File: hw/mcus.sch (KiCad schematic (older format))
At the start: 47 parts, among them P15 CONN_1, P16 CONN_1, P18 CONN_1, U10 MPU-6000, U11 HMC5983, U7 STM32F405VG, U8 STM32F303CC, U9 MS5611, X1 8MHz, X2 8MHz

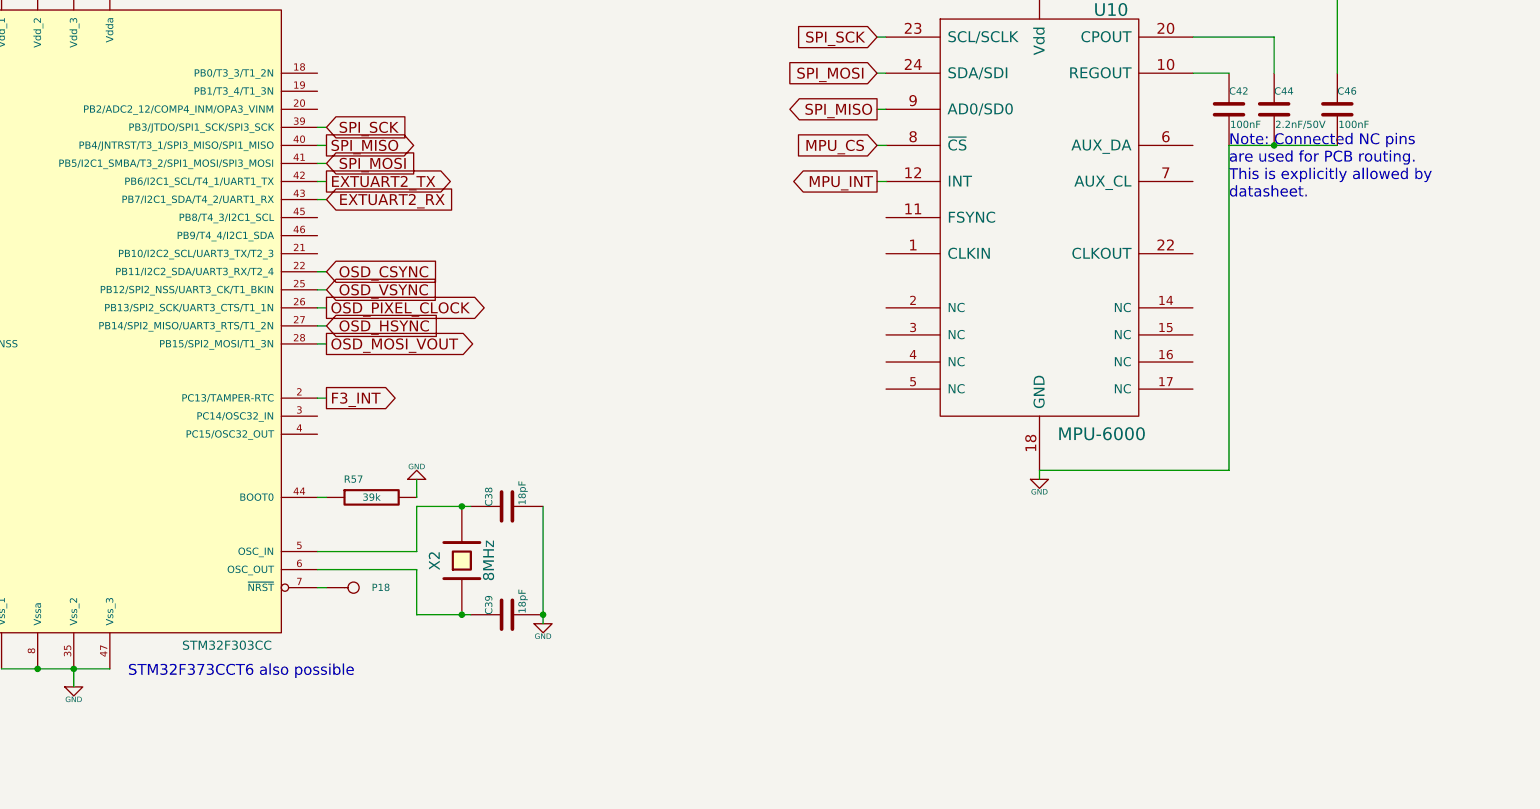
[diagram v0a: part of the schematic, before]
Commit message: Just cosmetic changes for eye-candy, no changes in board layout
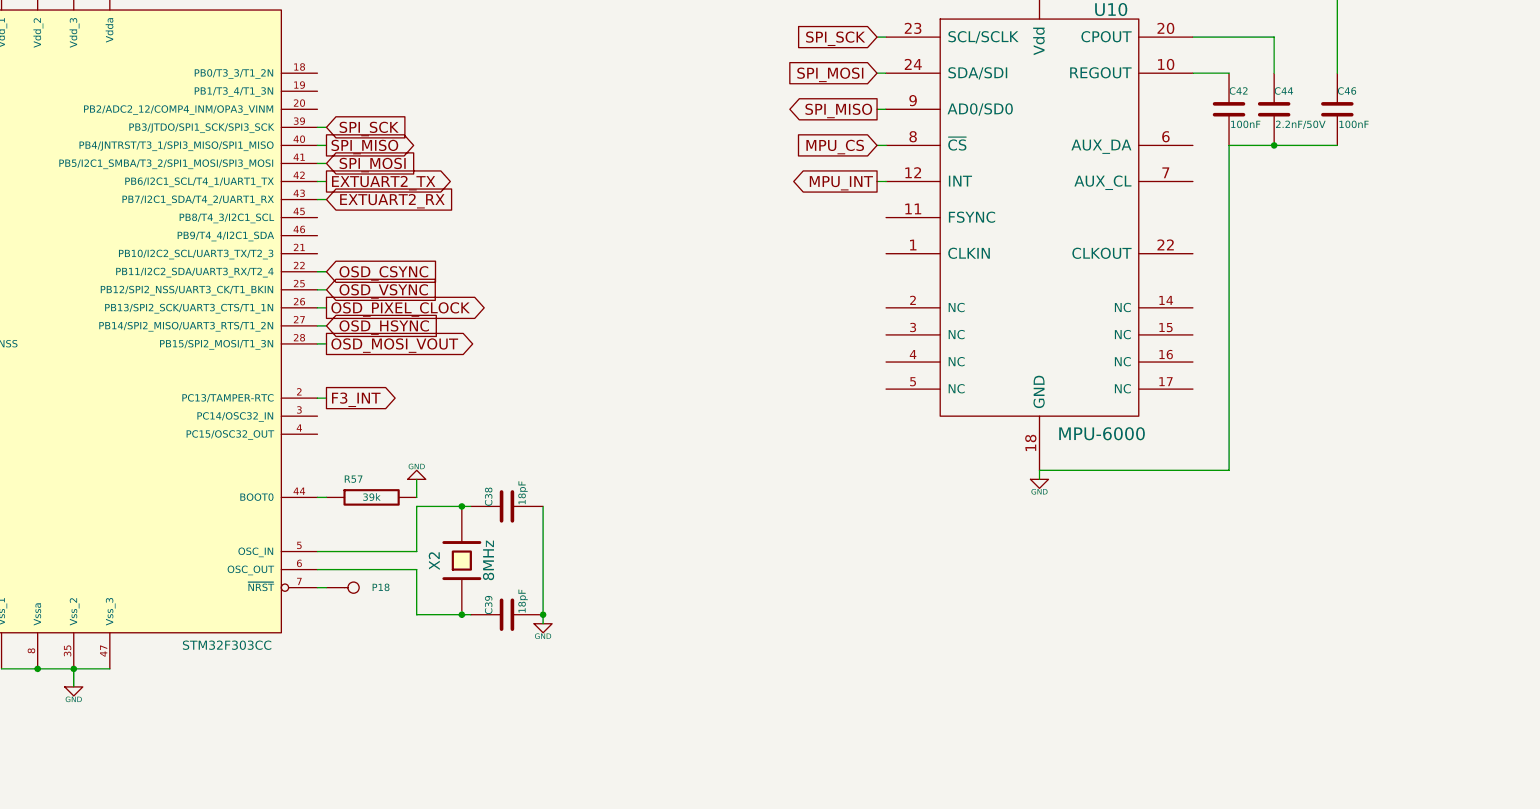
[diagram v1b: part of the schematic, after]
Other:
- note removed: "Note: Connected NC pins\nare used for PCB routing.\nThis is explicitly allowed by\ndatasheet."
- note removed: "STM32F373CCT6 also possible"
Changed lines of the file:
@@
 Sheet 3 3
 Title "DRACO - MCUs sheet"
-Date "10 nov 2013"
+Date "28 dec 2013"
 Rev "0.9"
 Comp "dandys"
@@
 Wire Wire Line
 	1800 6450 1850 6450
-Text Notes 14750 2600 0    60   ~ 0
-Note: Connected NC pins\nare used for PCB routing.\nThis is explicitly allowed by\ndatasheet.
 Wire Wire Line
 	9700 3000 9750 3000
@@
 Wire Wire Line
 	7650 6750 7650 6800
-Text Notes 8650 5250 0    60   ~ 0
-STM32F373CCT6 also possible
 Text Notes 3650 7350 0    60   ~ 0
 STM32F427VIT6 is better alternative

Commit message: Pixel clock (SPI SCK) connected to PB0 (TIM1) in schematic This will enable us to use both SPIs in slave mode with fine pixel clock tuning by timer TIM1
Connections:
- net OSD_PIXEL_CLOCK: now also U8.10 (PA0/WKUP/UART2_CTS/T2_1_ETR)
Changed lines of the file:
@@
 Sheet 3 3
 Title "DRACO - MCUs sheet"
-Date "26 jan 2014"
+Date "11 feb 2014"
 Rev "0.9"
 Comp "dandys"
@@
 Wire Wire Line
 	9700 3200 9750 3200
-Text GLabel 6650 2400 0    60   Input ~ 0
+Text GLabel 6500 2400 0    60   Input ~ 0
 OSD_PIXEL_CLOCK
 Wire Wire Line
-	6650 2400 6700 2400
+	6500 2400 6700 2400
 $Comp
 L R R62
@@
 Text Notes 3650 7350 0    60   ~ 0
 STM32F427VIT6 is better alternative
+Wire Wire Line
+	6600 2400 6600 1900
+Wire Wire Line
+	6600 1900 6700 1900
+Connection ~ 6600 2400
 $EndSCHEMATC

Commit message: schematics: preparations for board rev. 1.0 MPU-6000 and HMC5893 replaced by single chip solution MPU-9250 Added video sync tip clamping MAX4090
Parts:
- removed C41: 4.7uF, c_0805, symbol C
- removed C43: 100nF, c_0603, symbol C
- removed C44: 2.2nF/50V, c_0603, symbol C
- removed C45: 220nF, c_0603, symbol C
- removed R62: 39k, r_0603, symbol R
- removed U10: MPU-6000, dandys_qfn24, symbol MPU-6000
- removed U11: HMC5983, lpcc-16, symbol HMC5983
- added C49: 10nF, c_0603, symbol C
- added U13: MPU-9250, ~, symbol MPU-9250
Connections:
- net +3.3V: now also C46.1, C49.1, U13.1 (RESV-VDDIO), U13.13 (Vdd), U13.8 (Vddio)
- net +3.3VADC: no longer C46.1
- net GND: now also C49.2, U13.18 (GND), U13.20 (RESV-GND)
- net MPU_CS: now also U13.22 (~CS~)
- net MPU_INT: now also U13.12 (INT)
- net OSD_PIXEL_CLOCK: now also U8.18 (PB0/T3_3/T1_2N); no longer U8.10 (PA0/WKUP/UART2_CTS/T2_1_ETR)
- net SPI_MISO: now also U13.9 (AD0/SD0)
- net SPI_MOSI: now also U13.24 (SDA/SDI)
- net SPI_SCK: now also U13.23 (SCL/SCLK)
- net at C42.1: now also U13.10 (REGOUT)
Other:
- note added: "Gyro & accelerometer & magnetometer"
- note removed: "Gyro & accelerometer"
- note removed: "Magnetometer"
- moved on the sheet: C42, C46

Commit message: HW board revision 1.0
- HMC5983 and MPU6000 replaced by MPU9250 on SPI bus
- added video sync-tip clamping and buffer circuit MAX4090
- added shottky diode D1 as optional alternative for ideal diode circuit LTC4411
- SPI pixel clock generation now also connected to timer output for more fine clock tuning to be possible
- PWM11 and PWM12 signals now switched to PD12 and PD13 to avoid collision of timer usage for sonar echo measurement
- SMT32F4 LEDs moved to more suitable place on the board and blue LED switched to GPIO PC5 (was PE3)
- added micro button
- SWD pads for STM32F3 is now standard 2.54 pitch header
- added SPI flash MICRON N25Q032A13ESC40G
- added pulldown resistors for Q1, Q2
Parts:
- removed P15, P16: CONN_1, testpoint_pad, symbol CONN_1
- added C41: 100nF, c_0603, symbol C
- added P14: CONN_2, ~, symbol CONN_2
- added R62: 39k, r_0603, symbol R
- added SW2: EVQP7A01K, ~, symbol SW_PUSH
- added U10: FLASH-SPI-SO8, symbol FLASH-SPI-SO8
- U7: value STM32F405VG -> STM32F427VIT6
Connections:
- net +3.3V: now also C41.1, R62.2, U10.3 (~WP), U10.7 (~HOLD), U10.8 (VCC)
- net GND: now also C41.2, SW2.1, U10.4 (GND)
- net PWM11: now also U7.60 (PD13)
- net PWM12: now also U7.59 (PD12)
- net SPI_MISO: now also U10.2 (SO)
- net SPI_MOSI: now also U10.5 (SI)
- net SPI_SCK: now also U10.6 (SCK)
- net at U8.34 (PA13/JTMS/SWDIO): now also P14.2 (PM)
- net at U8.37 (PA14/JTCK/SWCLK): now also P14.1 (P1)
- net at U7.2 (PE3): no longer R54.2
- net at U7.34 (PC5): now also R54.2
- net at U7.77 (PA15-JTDI): now also SW2.2
- net HMC_CS renamed FLASH_CS
- net FLASH_CS: now also R62.1, U10.1 (~CS)
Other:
- note added: "LED_BLUE was here\nin rev. 0.9"
- note added: "Now just for PCB routing\nPWM is on PD12 and PD13"
- note removed: "STM32F427VIT6 is better alternative"
- moved on the sheet: D6, R54
